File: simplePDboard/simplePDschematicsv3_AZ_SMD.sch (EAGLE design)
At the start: 15 parts, among them IC1 TL071P

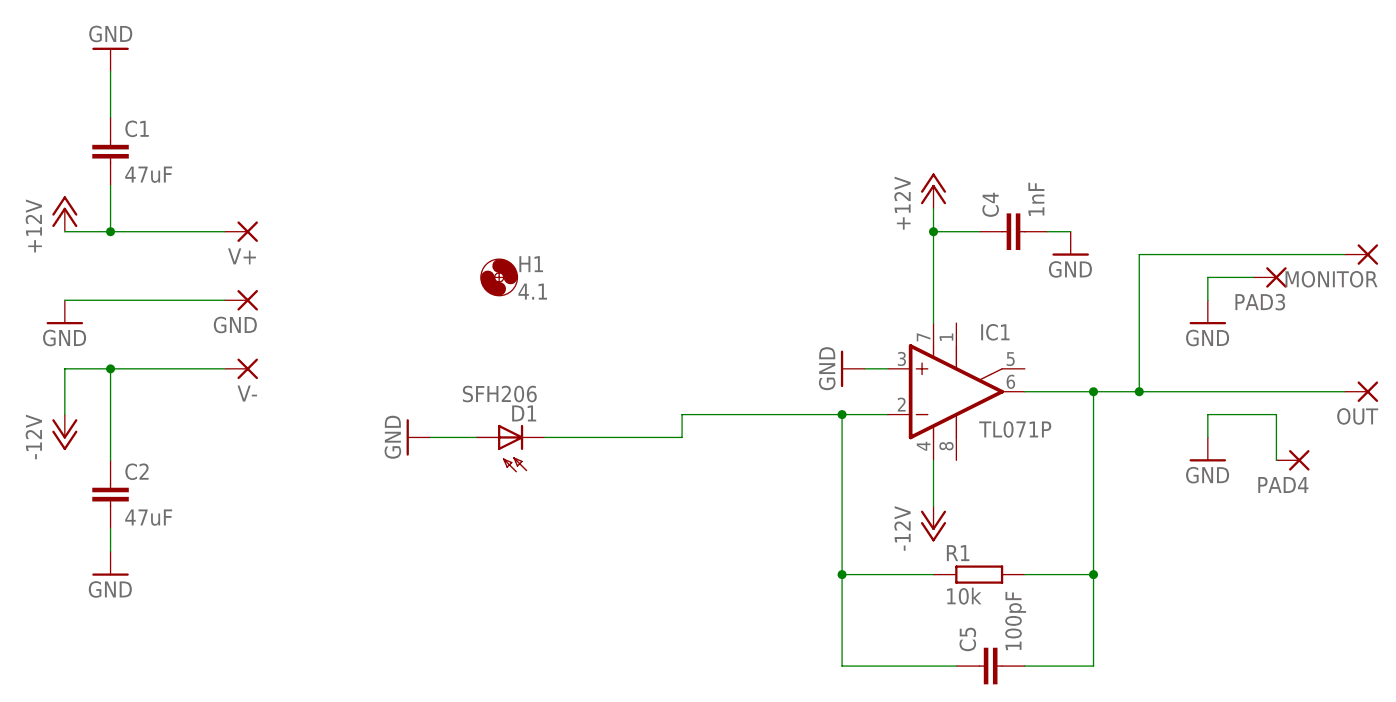
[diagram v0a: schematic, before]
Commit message: Updated the simplePD board. — It is not in photovoltaic mode. — The capacitors are better located. — We added a serial resistor for 50Ohm termination. — The power connectors are closer by.
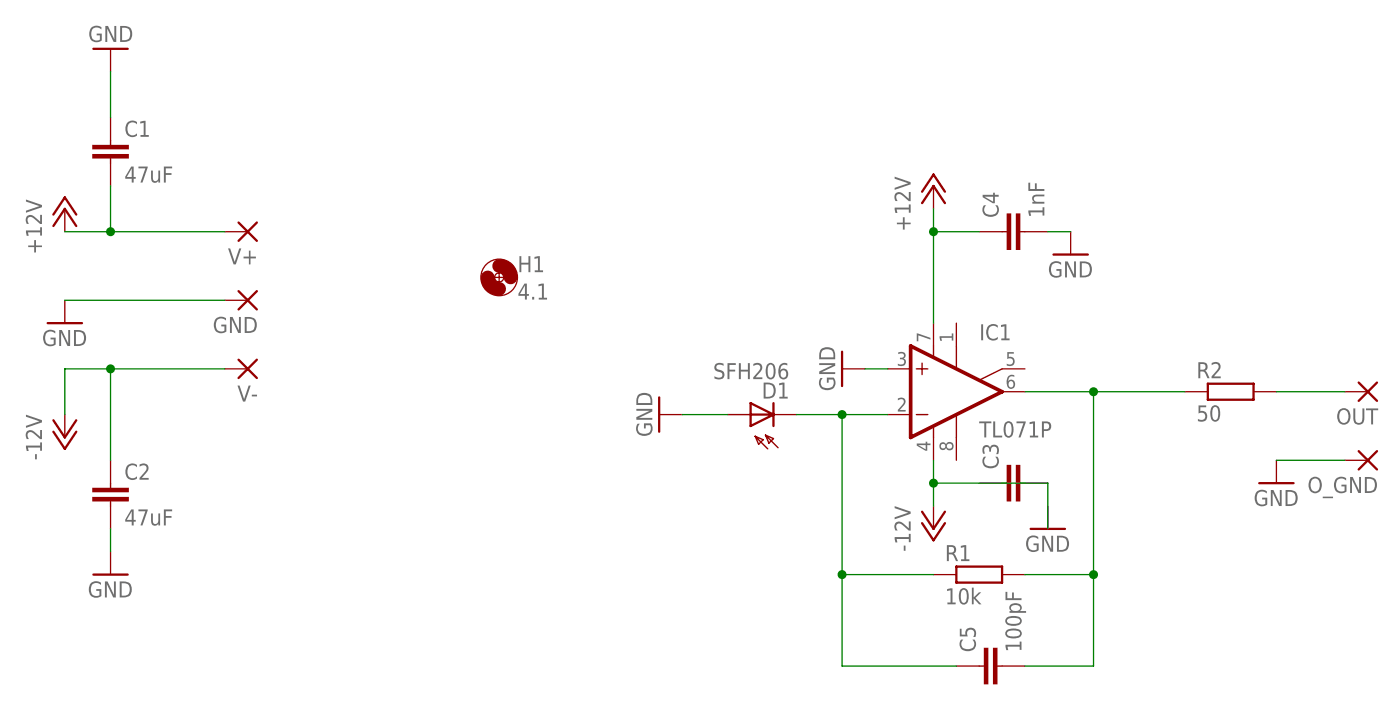
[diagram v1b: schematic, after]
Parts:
- removed MONITOR, PAD3, PAD4: (no value), wirepad:1,6/0,9
- added C3: (no value), resistor:C-EUC0504
- added O_GND: (no value), wirepad:1,6/0,9
- added R2: 50, resistor:R-EU_M1206
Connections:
- new net N$1: OUT.P, R2.2
- net GND: now also O_GND.P; no longer PAD3.P, PAD4.P
- net N$2: now also R2.1; no longer MONITOR.P, OUT.P
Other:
- moved on the sheet: D1
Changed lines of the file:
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@@
 <?xml version="1.0" encoding="utf-8"?>
 <!DOCTYPE eagle SYSTEM "eagle.dtd">
-<eagle version="6.6.0">
+<eagle version="7.5.0">
 <drawing>
 <settings>
@@
 <part name="R1" library="resistor" deviceset="R-EU_" device="M1206" value="10k"/>
 <part name="GND2" library="supply1" deviceset="GND" device=""/>
-<part name="GND3" library="supply1" deviceset="GND" device=""/>
 <part name="P+1" library="supply1" deviceset="+12V" device=""/>
 <part name="P-2" library="supply1" deviceset="-12V" device=""/>
@@
 <part name="GND6" library="supply1" deviceset="GND" device=""/>
 <part name="GND7" library="supply1" deviceset="GND" device=""/>
+<part name="GND8" library="supply1" deviceset="GND" device=""/>
 <part name="V+" library="wirepad" deviceset="1,6/0,9" device=""/>
 <part name="GND" library="wirepad" deviceset="1,6/0,9" device=""/>
@@
 <part name="H1" library="holes" deviceset="MOUNT-HOLE" device="4.1" value="4.1"/>
 <part name="FRAME1" library="frames" deviceset="A4L-LOC" device=""/>
-<part name="MONITOR" library="wirepad" deviceset="1,6/0,9" device=""/>
 <part name="OUT" library="wirepad" deviceset="1,6/0,9" device=""/>
-<part name="PAD3" library="wirepad" deviceset="1,6/0,9" device=""/>
-<part name="PAD4" library="wirepad" deviceset="1,6/0,9" device=""/>
+<part name="O_GND" library="wirepad" deviceset="1,6/0,9" device=""/>
 <part name="GND9" library="supply1" deviceset="GND" device=""/>
+<part name="R2" library="resistor" deviceset="R-EU_" device="M1206" value="50"/>
+<part name="C3" library="resistor" deviceset="C-EU" device="C0504"/>
 </parts>
 <sheets>
@@
 </plain>
 <instances>
-<instance part="D1" gate="1" x="106.68" y="86.36" rot="R90"/>
+<instance part="D1" gate="1" x="134.62" y="88.9" rot="R90"/>
 <instance part="IC1" gate="A" x="157.48" y="91.44"/>
 <instance part="GND1" gate="1" x="144.78" y="93.98" rot="R270"/>
 <instance part="R1" gate="G$1" x="160.02" y="71.12"/>
-<instance part="GND2" gate="1" x="185.42" y="83.82"/>
-<instance part="GND3" gate="1" x="185.42" y="99.06"/>
+<instance part="GND2" gate="1" x="193.04" y="81.28"/>
 <instance part="P+1" gate="1" x="154.94" y="114.3"/>
 <instance part="P-2" gate="1" x="154.94" y="76.2"/>
@@
 <instance part="GND6" gate="1" x="63.5" y="129.54" rot="R180"/>
 <instance part="GND7" gate="1" x="170.18" y="106.68"/>
+<instance part="GND8" gate="1" x="167.64" y="76.2"/>
 <instance part="V+" gate="1" x="78.74" y="109.22" rot="R180"/>
 <instance part="GND" gate="1" x="78.74" y="101.6" rot="R180"/>
@@
 <instance part="H1" gate="G$1" x="106.68" y="104.14"/>
 <instance part="FRAME1" gate="G$1" x="0" y="0"/>
-<instance part="MONITOR" gate="1" x="203.2" y="106.68" rot="R180"/>
 <instance part="OUT" gate="1" x="203.2" y="91.44" rot="R180"/>
-<instance part="PAD3" gate="1" x="193.04" y="104.14" rot="R180"/>
-<instance part="PAD4" gate="1" x="195.58" y="83.82" rot="R180"/>
-<instance part="GND9" gate="1" x="96.52" y="86.36" rot="R270"/>
+<instance part="O_GND" gate="1" x="203.2" y="83.82" rot="R180"/>
+<instance part="GND9" gate="1" x="124.46" y="88.9" rot="R270"/>
+<instance part="R2" gate="G$1" x="187.96" y="91.44"/>
+<instance part="C3" gate="G$1" x="162.56" y="81.28" rot="R90"/>
 </instances>
 <busses>
@@
 <segment>
 <pinref part="GND2" gate="1" pin="GND"/>
-<wire x1="185.42" y1="86.36" x2="185.42" y2="88.9" width="0.1524" layer="91"/>
-<pinref part="PAD4" gate="1" pin="P"/>
-<wire x1="193.04" y1="83.82" x2="193.04" y2="88.9" width="0.1524" layer="91"/>
-<wire x1="193.04" y1="88.9" x2="185.42" y2="88.9" width="0.1524" layer="91"/>
+<pinref part="O_GND" gate="1" pin="P"/>
+<wire x1="200.66" y1="83.82" x2="193.04" y2="83.82" width="0.1524" layer="91"/>
 </segment>
 <segment>
@@
 </segment>
 <segment>
-<pinref part="GND3" gate="1" pin="GND"/>
-<wire x1="185.42" y1="101.6" x2="185.42" y2="104.14" width="0.1524" layer="91"/>
-<pinref part="PAD3" gate="1" pin="P"/>
-<wire x1="185.42" y1="104.14" x2="190.5" y2="104.14" width="0.1524" layer="91"/>
-</segment>
-<segment>
 <pinref part="C2" gate="G$1" pin="2"/>
 <pinref part="GND5" gate="1" pin="GND"/>
@@
 </segment>
 <segment>
+<pinref part="D1" gate="1" pin="A"/>
 <pinref part="GND9" gate="1" pin="GND"/>
-<pinref part="D1" gate="1" pin="A"/>
-<wire x1="99.06" y1="86.36" x2="104.14" y2="86.36" width="0.1524" layer="91"/>
+<wire x1="132.08" y1="88.9" x2="127" y2="88.9" width="0.1524" layer="91"/>
 </segment>
 </net>
@@
 <pinref part="IC1" gate="A" pin="OUT"/>
 <wire x1="165.1" y1="91.44" x2="172.72" y2="91.44" width="0.1524" layer="91"/>
-<wire x1="172.72" y1="91.44" x2="177.8" y2="91.44" width="0.1524" layer="91"/>
-<wire x1="177.8" y1="91.44" x2="200.66" y2="91.44" width="0.1524" layer="91"/>
-<wire x1="200.66" y1="106.68" x2="177.8" y2="106.68" width="0.1524" layer="91"/>
-<wire x1="177.8" y1="106.68" x2="177.8" y2="91.44" width="0.1524" layer="91"/>
-<junction x="177.8" y="91.44"/>
+<wire x1="172.72" y1="91.44" x2="182.88" y2="91.44" width="0.1524" layer="91"/>
 <pinref part="R1" gate="G$1" pin="2"/>
 <wire x1="165.1" y1="71.12" x2="172.72" y2="71.12" width="0.1524" layer="91"/>
@@
 <pinref part="C5" gate="G$1" pin="2"/>
 <wire x1="172.72" y1="60.96" x2="165.1" y2="60.96" width="0.1524" layer="91"/>
-<pinref part="OUT" gate="1" pin="P"/>
-<pinref part="MONITOR" gate="1" pin="P"/>
+<pinref part="R2" gate="G$1" pin="1"/>
 </segment>
 </net>
@@
 <pinref part="IC1" gate="A" pin="V-"/>
 <pinref part="P-2" gate="1" pin="-12V"/>
-<wire x1="154.94" y1="83.82" x2="154.94" y2="78.74" width="0.1524" layer="91"/>
+<wire x1="154.94" y1="83.82" x2="154.94" y2="81.28" width="0.1524" layer="91"/>
+<wire x1="154.94" y1="81.28" x2="154.94" y2="78.74" width="0.1524" layer="91"/>
+<wire x1="154.94" y1="81.28" x2="167.64" y2="81.28" width="0.1524" layer="91"/>
+<junction x="154.94" y="81.28"/>
+<wire x1="167.64" y1="81.28" x2="167.64" y2="76.2" width="0.1524" layer="91"/>
 </segment>
 <segment>
@@
 <segment>
 <pinref part="D1" gate="1" pin="C"/>
-<wire x1="111.76" y1="86.36" x2="127" y2="86.36" width="0.1524" layer="91"/>
 <pinref part="IC1" gate="A" pin="-IN"/>
 <wire x1="144.78" y1="88.9" x2="149.86" y2="88.9" width="0.1524" layer="91"/>
@@
 <wire x1="144.78" y1="60.96" x2="157.48" y2="60.96" width="0.1524" layer="91"/>
 <junction x="144.78" y="71.12"/>
-<wire x1="144.78" y1="88.9" x2="127" y2="88.9" width="0.1524" layer="91"/>
+<wire x1="144.78" y1="88.9" x2="139.7" y2="88.9" width="0.1524" layer="91"/>
 <junction x="144.78" y="88.9"/>
-<wire x1="127" y1="86.36" x2="127" y2="88.9" width="0.1524" layer="91"/>
-</segment>
-</net>
+</segment>
+</net>
+<net name="N$1" class="0">
+<segment>
+<pinref part="OUT" gate="1" pin="P"/>
+<wire x1="193.04" y1="91.44" x2="200.66" y2="91.44" width="0.1524" layer="91"/>
+<pinref part="R2" gate="G$1" pin="2"/>
+</segment>
+</net>
